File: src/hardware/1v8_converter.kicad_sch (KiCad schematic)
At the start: 3 parts, among them U24 TPS7A2018PDQNR

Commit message: Changed footprints from 0603 to 0402
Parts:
- C66, C67: footprint Capacitor_SMD:C_0603_1608Metric -> Capacitor_SMD:C_0504_1310Metric
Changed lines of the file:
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@@
 			)
 		)
-		(property "Footprint" "Capacitor_SMD:C_0603_1608Metric"
+		(property "Footprint" "Capacitor_SMD:C_0504_1310Metric"
 			(at 166.0652 104.14 0)
 			(effects
@@
 			)
 		)
-		(property "Footprint" "Capacitor_SMD:C_0603_1608Metric"
+		(property "Footprint" "Capacitor_SMD:C_0504_1310Metric"
 			(at 136.1948 104.14 0)
 			(effects

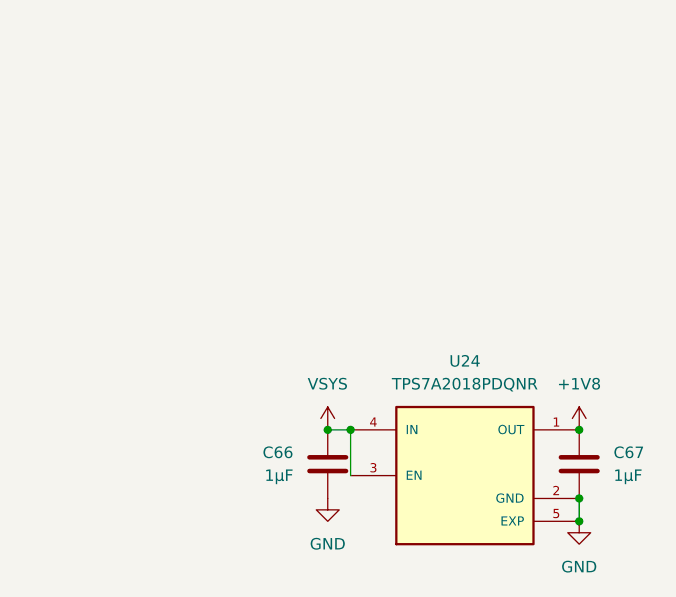
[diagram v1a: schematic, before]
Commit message: Replaced global labels with pin headers
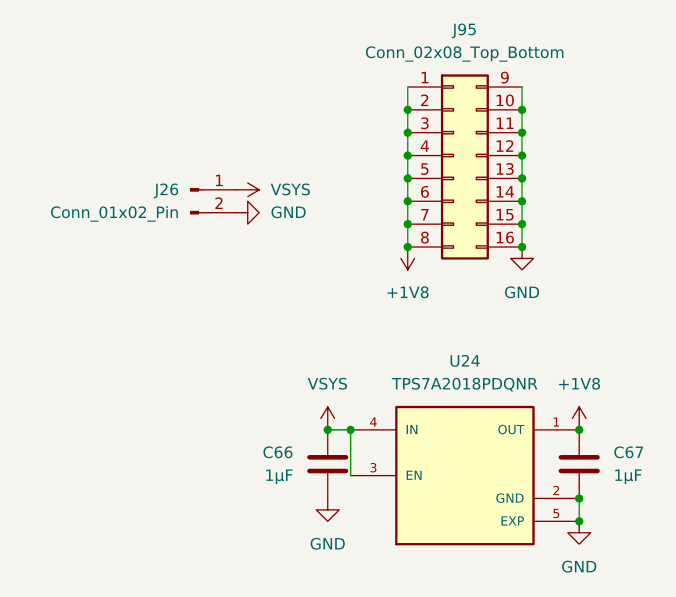
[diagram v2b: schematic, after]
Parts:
- added J26: Conn_01x02_Pin, symbol Connector:Conn_01x02_Pin
- added J95: Conn_02x08_Top_Bottom, symbol Connector_Generic:Conn_02x08_Top_Bottom
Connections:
- net +1V8: now also J95.1 (Pin_1), J95.2 (Pin_2), J95.3 (Pin_3), J95.4 (Pin_4), J95.5 (Pin_5), J95.6 (Pin_6), J95.7 (Pin_7), J95.8 (Pin_8)
- net GND: now also J26.2 (Pin_2), J95.10 (Pin_10), J95.11 (Pin_11), J95.12 (Pin_12), J95.13 (Pin_13), J95.14 (Pin_14), J95.15 (Pin_15), J95.16 (Pin_16), J95.9 (Pin_9)
- net VSYS: now also J26.1 (Pin_1)

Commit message: Reannotated schematic
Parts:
- renumbered C66 to C61, C67 to C62, J26 to J69, J95 to J70, U24 to U25
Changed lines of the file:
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@@
 		(dnp no)
 		(fields_autoplaced yes)
-		(property "Reference" "#PWR0343"
+		(property "Reference" "#PWR0370"
 			(at 165.1 113.03 0)
 			(effects
@@
 			(project "raywatch"
 				(path "/7b654ee8-2a53-4d39-8b7d-32c7bb3cb0ed/b8c5e1e6-da5e-4fb2-8283-82eb932a0e50"
-					(reference "#PWR0343")
+					(reference "#PWR0370")
 					(unit 1)
 				)
@@
 		(dnp no)
 		(fields_autoplaced yes)
-		(property "Reference" "C67"
+		(property "Reference" "C62"
 			(at 168.91 99.0599 0)
 			(effects
@@
 			(project "raywatch"
 				(path "/7b654ee8-2a53-4d39-8b7d-32c7bb3cb0ed/b8c5e1e6-da5e-4fb2-8283-82eb932a0e50"
-					(reference "C67")
+					(reference "C62")
 					(unit 1)
 				)
@@
 		(dnp no)
 		(fields_autoplaced yes)
-		(property "Reference" "#PWR0340"
+		(property "Reference" "#PWR0365"
 			(at 137.16 100.33 0)
 			(effects
@@
 			(project "raywatch"
 				(path "/7b654ee8-2a53-4d39-8b7d-32c7bb3cb0ed/b8c5e1e6-da5e-4fb2-8283-82eb932a0e50"
-					(reference "#PWR0340")
+					(reference "#PWR0365")
 					(unit 1)
 				)
@@
 		(dnp no)
 		(fields_autoplaced yes)
-		(property "Reference" "U24"
+		(property "Reference" "U25"
 			(at 152.4 88.9 0)
 			(effects
@@
 			(project "raywatch"
 				(path "/7b654ee8-2a53-4d39-8b7d-32c7bb3cb0ed/b8c5e1e6-da5e-4fb2-8283-82eb932a0e50"
-					(reference "U24")
+					(reference "U25")
 					(unit 1)
 				)
@@
 		(dnp no)
 		(fields_autoplaced yes)
-		(property "Reference" "#PWR059"
+		(property "Reference" "#PWR0367"
 			(at 146.05 72.39 0)
 			(effects
@@
 			(project "raywatch"
 				(path "/7b654ee8-2a53-4d39-8b7d-32c7bb3cb0ed/b8c5e1e6-da5e-4fb2-8283-82eb932a0e50"
-					(reference "#PWR059")
+					(reference "#PWR0367")
 					(unit 1)
 				)
@@
 		(dnp no)
 		(fields_autoplaced yes)
-		(property "Reference" "#PWR0456"
+		(property "Reference" "#PWR0364"
 			(at 133.35 72.39 0)
 			(effects
@@
 			(project "raywatch"
 				(path "/7b654ee8-2a53-4d39-8b7d-32c7bb3cb0ed/b8c5e1e6-da5e-4fb2-8283-82eb932a0e50"
-					(reference "#PWR0456")
+					(reference "#PWR0364")
 					(unit 1)
 				)
@@
 		(dnp no)
 		(fields_autoplaced yes)
-		(property "Reference" "#PWR0455"
+		(property "Reference" "#PWR0363"
 			(at 123.19 69.85 0)
 			(effects
@@
 			(project "raywatch"
 				(path "/7b654ee8-2a53-4d39-8b7d-32c7bb3cb0ed/b8c5e1e6-da5e-4fb2-8283-82eb932a0e50"
-					(reference "#PWR0455")
+					(reference "#PWR0363")
 					(unit 1)
 				)
@@
 		(dnp no)
 		(fields_autoplaced yes)
-		(property "Reference" "J26"
+		(property "Reference" "J69"
 			(at 120.65 69.8499 0)
 			(effects
@@
 			(project "raywatch"
 				(path "/7b654ee8-2a53-4d39-8b7d-32c7bb3cb0ed/b8c5e1e6-da5e-4fb2-8283-82eb932a0e50"
-					(reference "J26")
+					(reference "J69")
 					(unit 1)
 				)
@@
 		(dnp no)
 		(fields_autoplaced yes)
-		(property "Reference" "#PWR0341"
+		(property "Reference" "#PWR0366"
 			(at 137.16 110.49 0)
 			(effects
@@
 			(project "raywatch"
 				(path "/7b654ee8-2a53-4d39-8b7d-32c7bb3cb0ed/b8c5e1e6-da5e-4fb2-8283-82eb932a0e50"
-					(reference "#PWR0341")
+					(reference "#PWR0366")
 					(unit 1)
 				)
@@
 		(dnp no)
 		(fields_autoplaced yes)
-		(property "Reference" "J95"
+		(property "Reference" "J70"
 			(at 152.4 52.07 0)
 			(effects
@@
 			(project "raywatch"
 				(path "/7b654ee8-2a53-4d39-8b7d-32c7bb3cb0ed/b8c5e1e6-da5e-4fb2-8283-82eb932a0e50"
-					(reference "J95")
+					(reference "J70")
 					(unit 1)
 				)
@@
 		(dnp no)
 		(fields_autoplaced yes)
-		(property "Reference" "C66"
+		(property "Reference" "C61"
 			(at 133.35 99.0599 0)
 			(effects
@@
 			(project "raywatch"
 				(path "/7b654ee8-2a53-4d39-8b7d-32c7bb3cb0ed/b8c5e1e6-da5e-4fb2-8283-82eb932a0e50"
-					(reference "C66")
+					(reference "C61")
 					(unit 1)
 				)
@@
 		(dnp no)
 		(fields_autoplaced yes)
-		(property "Reference" "#PWR0342"
+		(property "Reference" "#PWR0369"
 			(at 165.1 100.33 0)
 			(effects
@@
 			(project "raywatch"
 				(path "/7b654ee8-2a53-4d39-8b7d-32c7bb3cb0ed/b8c5e1e6-da5e-4fb2-8283-82eb932a0e50"
-					(reference "#PWR0342")
+					(reference "#PWR0369")
 					(unit 1)
 				)
@@
 		(dnp no)
 		(fields_autoplaced yes)
-		(property "Reference" "#PWR062"
+		(property "Reference" "#PWR0368"
 			(at 158.75 82.55 0)
 			(effects
@@
 			(project "raywatch"
 				(path "/7b654ee8-2a53-4d39-8b7d-32c7bb3cb0ed/b8c5e1e6-da5e-4fb2-8283-82eb932a0e50"
-					(reference "#PWR062")
-					(unit 1)
-				)
+					(reference "#PWR0368")
+					(unit 1)
+				)

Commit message: Assigned pin header footprints
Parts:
- J69: footprint (none) -> Connector_PinHeader_2.54mm:PinHeader_1x02_P2.54mm_Horizontal
- J70: footprint (none) -> Connector_PinHeader_2.54mm:PinHeader_1x16_P2.54mm_Vertical
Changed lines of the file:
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@@
 			)
 		)
-		(property "Footprint" ""
+		(property "Footprint" "Connector_PinHeader_2.54mm:PinHeader_1x02_P2.54mm_Horizontal"
 			(at 121.92 69.85 0)
 			(effects
@@
 			)
 		)
-		(property "Footprint" ""
+		(property "Footprint" "Connector_PinHeader_2.54mm:PinHeader_1x16_P2.54mm_Vertical"
 			(at 151.13 66.04 0)
 			(effects

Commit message: Fixed footprints
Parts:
- J70: footprint Connector_PinHeader_2.54mm:PinHeader_1x16_P2.54mm_Vertical -> Connector_PinHeader_2.54mm:PinHeader_2x08_P2.54mm_Vertical
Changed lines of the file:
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@@
 			)
 		)
-		(property "Footprint" "Connector_PinHeader_2.54mm:PinHeader_1x16_P2.54mm_Vertical"
+		(property "Footprint" "Connector_PinHeader_2.54mm:PinHeader_2x08_P2.54mm_Vertical"
 			(at 151.13 66.04 0)
 			(effects

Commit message: Changed pin headers to vertical
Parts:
- J69: footprint Connector_PinHeader_2.54mm:PinHeader_1x02_P2.54mm_Horizontal -> Connector_PinHeader_2.54mm:PinHeader_1x02_P2.54mm_Vertical
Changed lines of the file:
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@@
 			)
 		)
-		(property "Footprint" "Connector_PinHeader_2.54mm:PinHeader_1x02_P2.54mm_Horizontal"
+		(property "Footprint" "Connector_PinHeader_2.54mm:PinHeader_1x02_P2.54mm_Vertical"
 			(at 121.92 69.85 0)
 			(effects

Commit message: Fixed connector footprints; Changed conectors from 2.54 to 1.27
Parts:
- J67: renamed from J69; footprint Connector_PinHeader_2.54mm:PinHeader_1x02_P2.54mm_Vertical -> Connector_PinHeader_1.27mm:PinHeader_1x02_P1.27mm_Vertical
- J68: renamed from J70; footprint Connector_PinHeader_2.54mm:PinHeader_2x08_P2.54mm_Vertical -> Connector_PinHeader_1.27mm:PinHeader_2x08_P1.27mm_Vertical
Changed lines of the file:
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@@
 		(dnp no)
 		(fields_autoplaced yes)
-		(property "Reference" "#PWR0372"
+		(property "Reference" "#PWR0374"
 			(at 165.1 113.03 0)
 			(effects
@@
 			(project "raywatch"
 				(path "/7b654ee8-2a53-4d39-8b7d-32c7bb3cb0ed/b8c5e1e6-da5e-4fb2-8283-82eb932a0e50"
-					(reference "#PWR0372")
+					(reference "#PWR0374")
 					(unit 1)
 				)
@@
 		(dnp no)
 		(fields_autoplaced yes)
-		(property "Reference" "#PWR0367"
+		(property "Reference" "#PWR0369"
 			(at 137.16 100.33 0)
 			(effects
@@
 			(project "raywatch"
 				(path "/7b654ee8-2a53-4d39-8b7d-32c7bb3cb0ed/b8c5e1e6-da5e-4fb2-8283-82eb932a0e50"
-					(reference "#PWR0367")
+					(reference "#PWR0369")
 					(unit 1)
 				)
@@
 		(dnp no)
 		(fields_autoplaced yes)
-		(property "Reference" "#PWR0369"
+		(property "Reference" "#PWR0371"
 			(at 146.05 72.39 0)
 			(effects
@@
 			(project "raywatch"
 				(path "/7b654ee8-2a53-4d39-8b7d-32c7bb3cb0ed/b8c5e1e6-da5e-4fb2-8283-82eb932a0e50"
-					(reference "#PWR0369")
+					(reference "#PWR0371")
 					(unit 1)
 				)
@@
 		(dnp no)
 		(fields_autoplaced yes)
-		(property "Reference" "#PWR0366"
+		(property "Reference" "#PWR0368"
 			(at 133.35 72.39 0)
 			(effects
@@
 			(project "raywatch"
 				(path "/7b654ee8-2a53-4d39-8b7d-32c7bb3cb0ed/b8c5e1e6-da5e-4fb2-8283-82eb932a0e50"
-					(reference "#PWR0366")
+					(reference "#PWR0368")
 					(unit 1)
 				)
@@
 		(dnp no)
 		(fields_autoplaced yes)
-		(property "Reference" "#PWR0365"
+		(property "Reference" "#PWR0367"
 			(at 123.19 69.85 0)
 			(effects
@@
 			(project "raywatch"
 				(path "/7b654ee8-2a53-4d39-8b7d-32c7bb3cb0ed/b8c5e1e6-da5e-4fb2-8283-82eb932a0e50"
-					(reference "#PWR0365")
+					(reference "#PWR0367")
 					(unit 1)
 				)
@@
 		(dnp no)
 		(fields_autoplaced yes)
-		(property "Reference" "J69"
+		(property "Reference" "J67"
 			(at 120.65 69.8499 0)
 			(effects
@@
 			)
 		)
-		(property "Footprint" "Connector_PinHeader_2.54mm:PinHeader_1x02_P2.54mm_Vertical"
+		(property "Footprint" "Connector_PinHeader_1.27mm:PinHeader_1x02_P1.27mm_Vertical"
 			(at 121.92 69.85 0)
 			(effects
@@
 			(project "raywatch"
 				(path "/7b654ee8-2a53-4d39-8b7d-32c7bb3cb0ed/b8c5e1e6-da5e-4fb2-8283-82eb932a0e50"
-					(reference "J69")
+					(reference "J67")
 					(unit 1)
 				)
@@
 		(dnp no)
 		(fields_autoplaced yes)
-		(property "Reference" "#PWR0368"
+		(property "Reference" "#PWR0370"
 			(at 137.16 110.49 0)
 			(effects
@@
 			(project "raywatch"
 				(path "/7b654ee8-2a53-4d39-8b7d-32c7bb3cb0ed/b8c5e1e6-da5e-4fb2-8283-82eb932a0e50"
-					(reference "#PWR0368")
+					(reference "#PWR0370")
 					(unit 1)
 				)
@@
 		(dnp no)
 		(fields_autoplaced yes)
-		(property "Reference" "J70"
+		(property "Reference" "J68"
 			(at 152.4 52.07 0)
 			(effects
@@
 			)
 		)
-		(property "Footprint" "Connector_PinHeader_2.54mm:PinHeader_2x08_P2.54mm_Vertical"
+		(property "Footprint" "Connector_PinHeader_1.27mm:PinHeader_2x08_P1.27mm_Vertical"
 			(at 151.13 66.04 0)
 			(effects
@@
 			(project "raywatch"
 				(path "/7b654ee8-2a53-4d39-8b7d-32c7bb3cb0ed/b8c5e1e6-da5e-4fb2-8283-82eb932a0e50"
-					(reference "J70")
+					(reference "J68")
 					(unit 1)
 				)
@@
 		(dnp no)
 		(fields_autoplaced yes)
-		(property "Reference" "#PWR0371"
+		(property "Reference" "#PWR0373"
 			(at 165.1 100.33 0)
 			(effects
@@
 			(project "raywatch"
 				(path "/7b654ee8-2a53-4d39-8b7d-32c7bb3cb0ed/b8c5e1e6-da5e-4fb2-8283-82eb932a0e50"
-					(reference "#PWR0371")
+					(reference "#PWR0373")
 					(unit 1)
 				)
@@
 		(dnp no)
 		(fields_autoplaced yes)
-		(property "Reference" "#PWR0370"
+		(property "Reference" "#PWR0372"
 			(at 158.75 82.55 0)
 			(effects
@@
 			(project "raywatch"
 				(path "/7b654ee8-2a53-4d39-8b7d-32c7bb3cb0ed/b8c5e1e6-da5e-4fb2-8283-82eb932a0e50"
-					(reference "#PWR0370")
-					(unit 1)
-				)
+					(reference "#PWR0372")
+					(unit 1)
+				)
